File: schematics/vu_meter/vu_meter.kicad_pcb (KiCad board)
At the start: 2 copper layers, 116.1 x 50 mm, 58 parts, among them J1 Pwr_Signal, U1 LM833N, U2 LM339, U3 LM339, U4 LM339

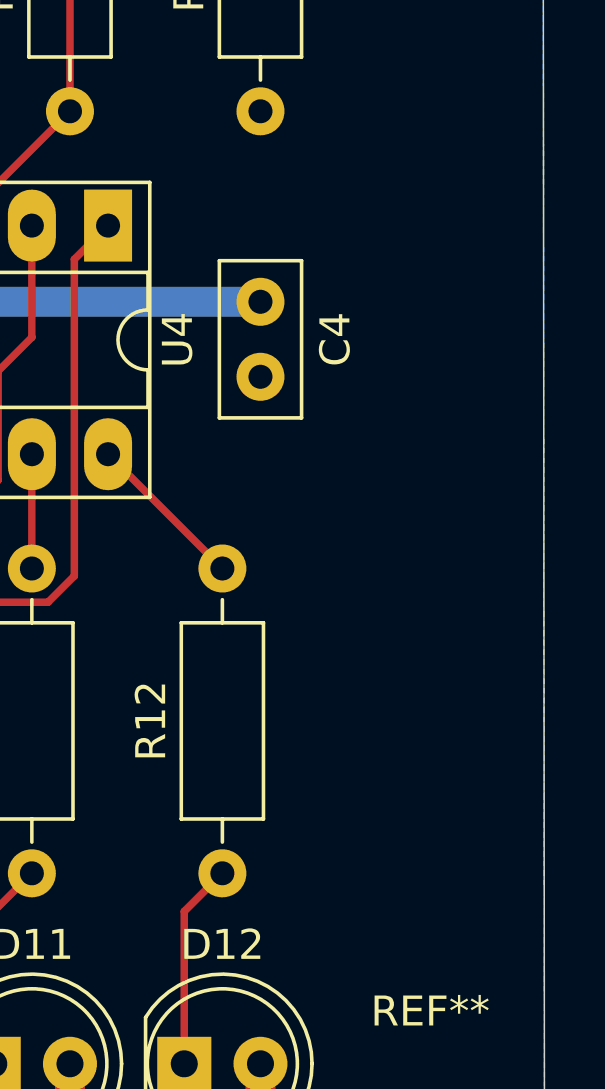
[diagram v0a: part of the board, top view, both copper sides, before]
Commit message: Schematic Main: Add corrected headphone amp
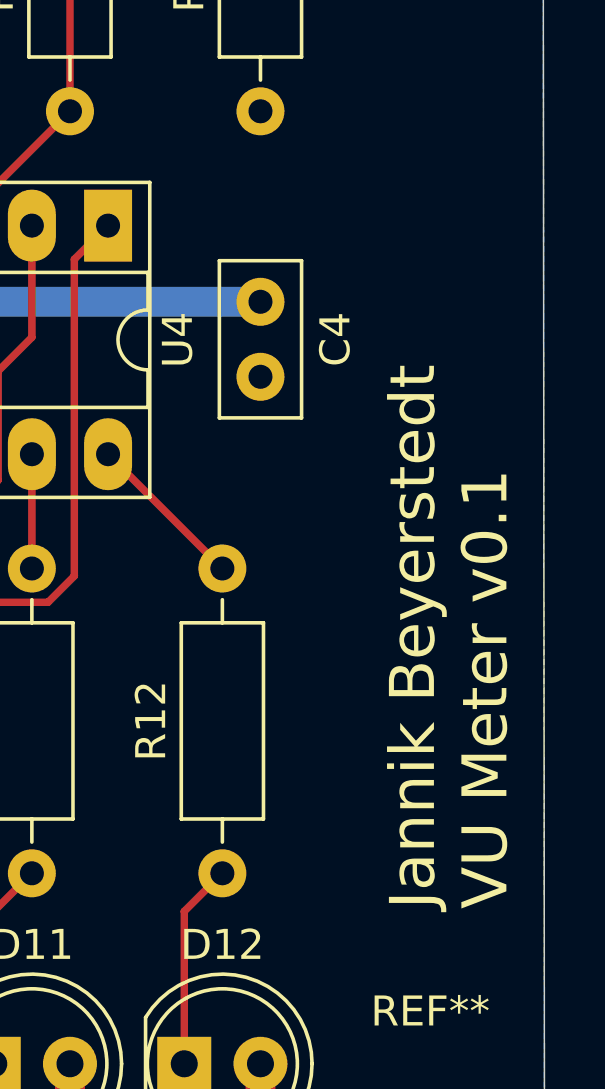
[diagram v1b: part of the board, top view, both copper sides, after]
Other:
- board text added: "Jannik Beyerstedt VU Meter v0.1"

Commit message: final fixes for first prototype PCB order
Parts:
- removed REF** (x4): MountingHole_3.2mm_M3, MountingHole:MountingHole_3.2mm_M3
- C5: footprint Capacitor_THT:CP_Radial_D10.0mm_P5.00mm -> Capacitor_THT:CP_Radial_D5.0mm_P2.50mm
- C6: footprint Capacitor_THT:CP_Radial_D10.0mm_P5.00mm -> Capacitor_THT:CP_Radial_D10.0mm_P2.50mm_P5.00mm
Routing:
- net Net-(R110-Pad1): track 25.2 -> 12.8 mm
- net Net-(R106-Pad1): track 25.2 -> 12.8 mm
- net Net-(C5-Pad2): track 8.53 -> 11.0 mm
- net Net-(C6-Pad1): track 173.1 -> 175.6 mm
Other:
- net class Default: clearance 0.2 -> 0.25
- net class Power: clearance 0.2 -> 0.3
- rule trace_clearance: 0.2 -> 0.25
- board text added: "Sig,GND,+15V"

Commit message: VU meter: add -15V, fix footprints, specify LED resistors
TODO: Decide on signal smoothing
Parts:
- added C7: 100nF, Capacitor_THT:C_Disc_D5.0mm_W2.5mm_P5.00mm, F.Cu at (58.4, 38.7)
- added H1: MountingHole, MountingHole:MountingHole_3.2mm_M3_ISO14580, F.Cu at (34.0, 66.0)
- added H2: MountingHole, MountingHole:MountingHole_3.2mm_M3_ISO14580, F.Cu at (142.0, 66.0)
- added H3: MountingHole, MountingHole:MountingHole_3.2mm_M3_ISO14580, F.Cu at (142.0, 24.0)
- added H4: MountingHole, MountingHole:MountingHole_3.2mm_M3_ISO14580, F.Cu at (34.0, 24.0)
- C1, C2, C3, C4: footprint Capacitor_THT:C_Disc_D5.0mm_W2.5mm_P2.50mm -> Capacitor_THT:C_Disc_D5.0mm_W2.5mm_P5.00mm
- C5: value 10uF -> 1uF
- C6: value 2.2uF -> 47uF
- J1: footprint Connector_PinHeader_2.54mm:PinHeader_1x03_P2.54mm_Vertical -> Connector_PinHeader_2.54mm:PinHeader_1x04_P2.54mm_Vertical
- R1, R10, R11, R12, R2, R3, R4, R5, R6, R7, R8, R9: value R -> 390R
- R15: value 10K -> 100K
- RV1: footprint Potentiometer_THT:Potentiometer_Vishay_148-149_Single_Horizontal -> Potentiometer_THT:Potentiometer_Vishay_T73XX_Horizontal
- moved R13 3.42 mm to (55.2, 60.3)
- moved J1 3.24 mm to (57.8, 66.0), turned to 270 degrees
- moved C1 2.54 mm to (40.0, 41.3)
- moved D13 2.48 mm to (40.1, 47.0)
- moved D14 2.48 mm to (34.1, 33.0)
- moved R14 2.48 mm to (34.1, 47.0)
- moved C5 1.42 mm to (47.6, 55.2)
- moved RV1 1.27 mm to (44.5, 64.1)
- moved C2 0.55 mm to (85.1, 39.4)
- moved C3 0.55 mm to (111.2, 39.4)
- moved C4 0.55 mm to (136.6, 39.4)
- moved U2 0.06 mm to (80.6, 36.3)
- moved U4 0.06 mm to (131.4, 36.3)
- moved U3 0.05 mm to (106.0, 36.3)
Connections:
- J1 pad 1: +15V -> GNDREF
- J1 pad 2: Line_Input -> -15V
- J1 pad 3: GNDREF -> +15V
- U1 pad 4: GNDREF -> -15V
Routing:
- net -15V: track 0.00 -> 30.0 mm
- net Net-(R110-Pad1): track 12.8 -> 25.2 mm
- net Net-(R106-Pad1): track 12.8 -> 25.2 mm
- net Line_Input: track 17.6 -> 7.62 mm
- net +15V: track 266.0 -> 274.2 mm
- net Net-(D13-Pad2): track 41.6 -> 35.8 mm
- net Net-(C5-Pad1): track 11.4 -> 16.4 mm
- net Net-(C6-Pad1): track 175.6 -> 173.7 mm
- net Net-(C5-Pad2): track 11.0 -> 9.46 mm
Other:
- board text added: "Sig,-15,+15,GND"
- board text removed: "Sig,GND,+15V"

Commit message: Main: Add 15V phantom power
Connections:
- net GNDREF renamed GND

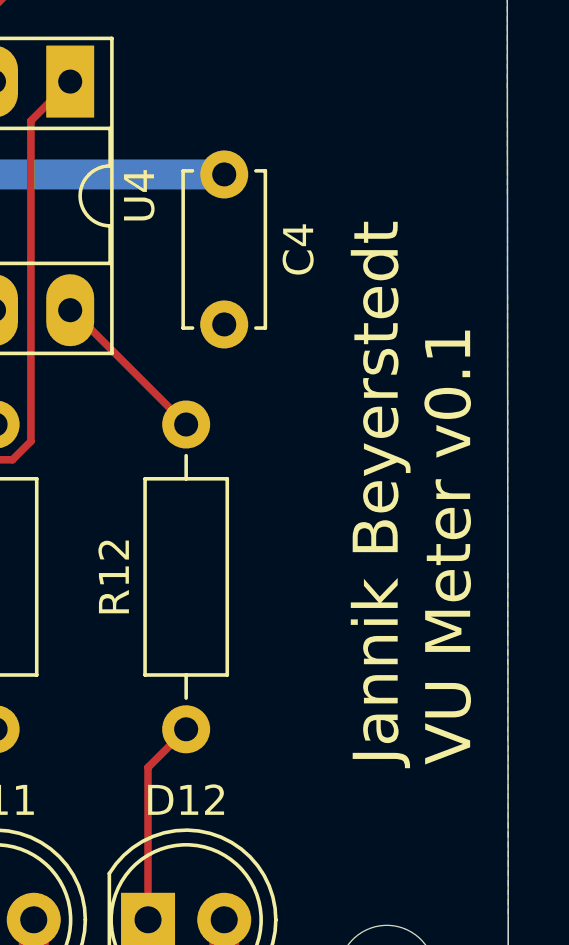
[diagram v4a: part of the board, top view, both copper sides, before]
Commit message: [TIDY] Channel Strip: Integrate VU Meter
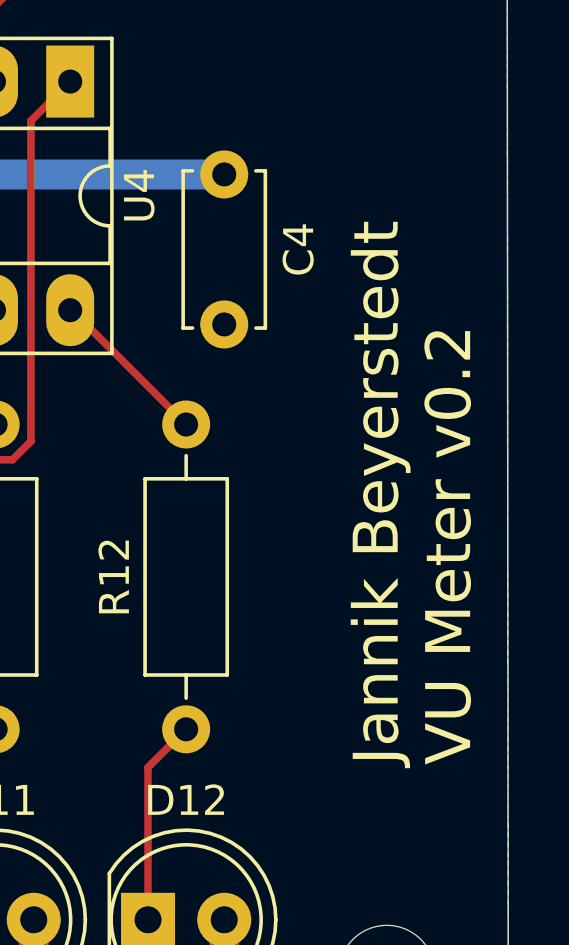
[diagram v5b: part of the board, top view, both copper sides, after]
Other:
- board text added: "Jannik Beyerstedt VU Meter v0.2"
- board text removed: "Jannik Beyerstedt VU Meter v0.1"
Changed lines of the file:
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@@
-(kicad_pcb (version 20171130) (host pcbnew "(5.1.8-0-10_14)")
+(kicad_pcb (version 20171130) (host pcbnew "(5.1.10-1-10_14)")
   (general
     (thickness 1.6)
@@
     (effects (font (size 1 1) (thickness 0.15)))
   )
-  (gr_text "Jannik Beyerstedt\nVU Meter v0.1" (at 142.875 59.055 90) (layer F.SilkS)
+  (gr_text "Jannik Beyerstedt\nVU Meter v0.2" (at 142.875 59.055 90) (layer F.SilkS)
     (effects (font (size 1.5 1.5) (thickness 0.3)) (justify left))
   )
